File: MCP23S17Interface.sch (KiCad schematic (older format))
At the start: 8 parts, among them J1 Conn_01x09, J2 Conn_01x16, J3 Conn_01x03, J4 Conn_01x03, J5 Conn_01x03, U1 MCP23S17_SP

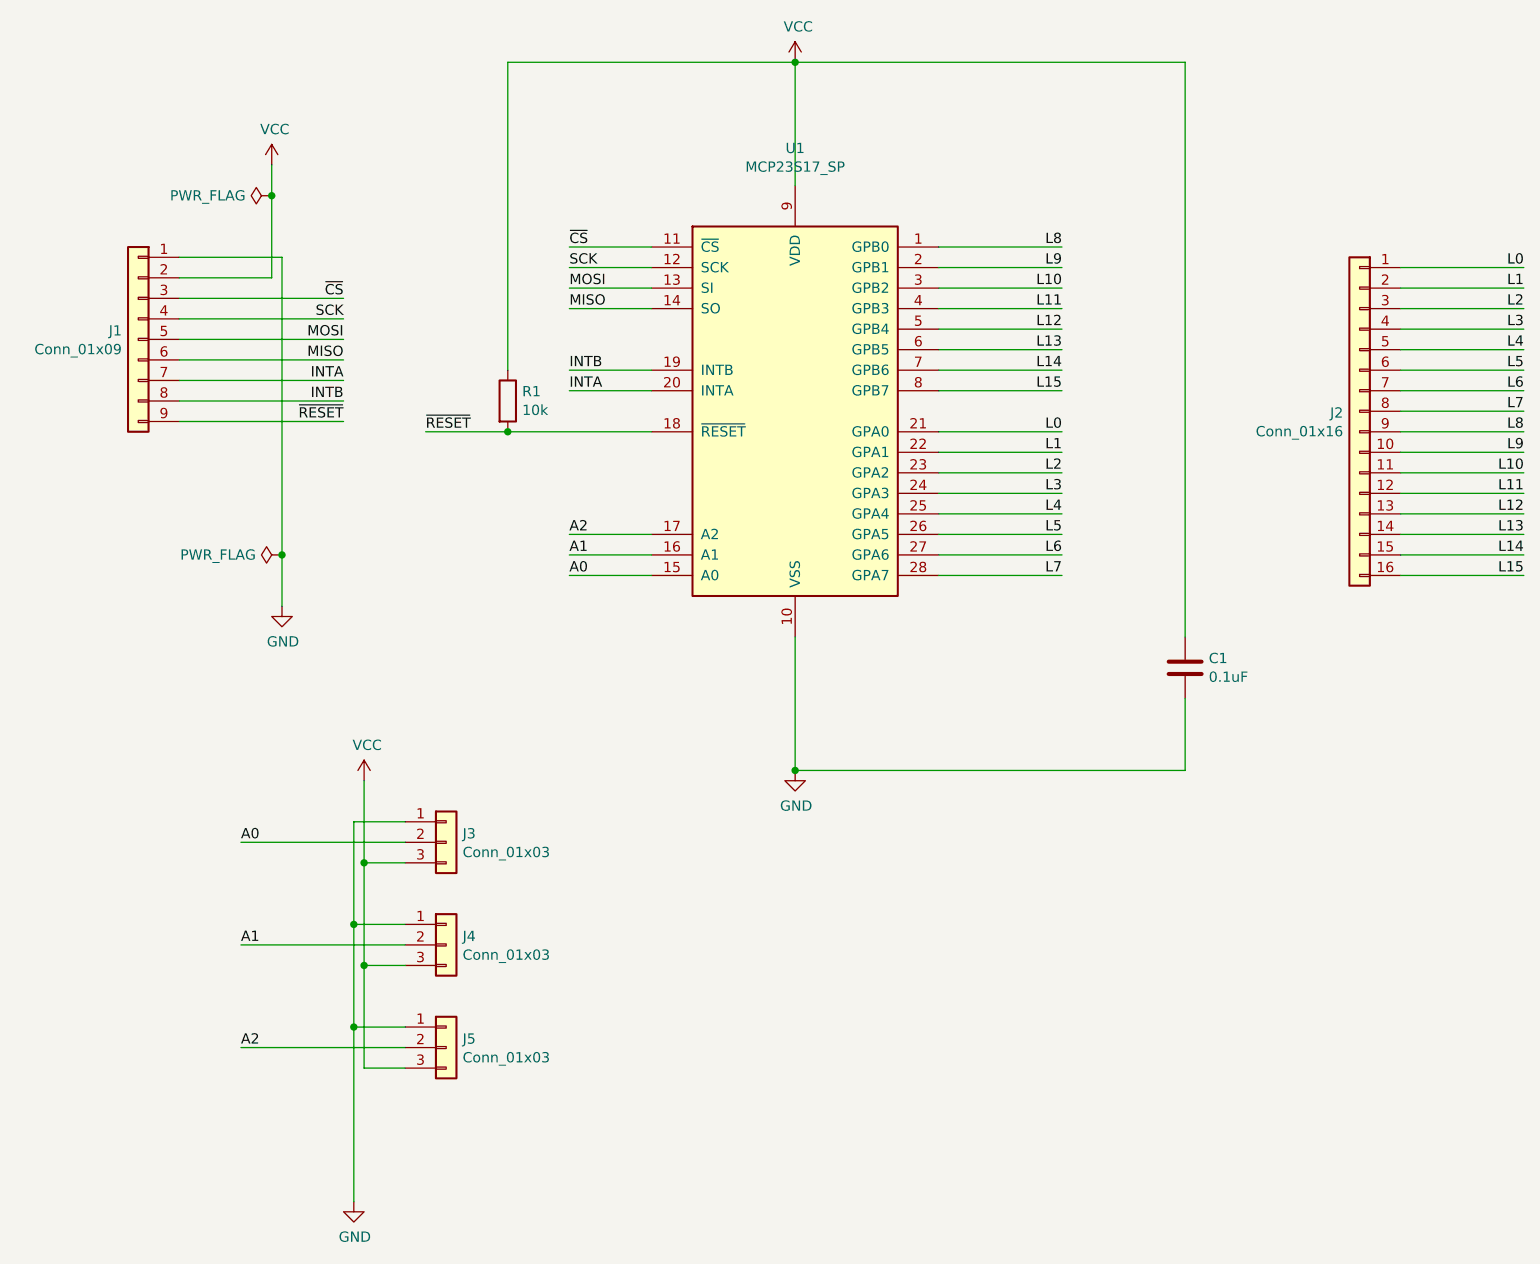
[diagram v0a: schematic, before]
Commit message: Replace the jumpered address selection with a dip switch box
Also, a 10k x 4 pull up resistor network in place of several 805 10k
resistors.
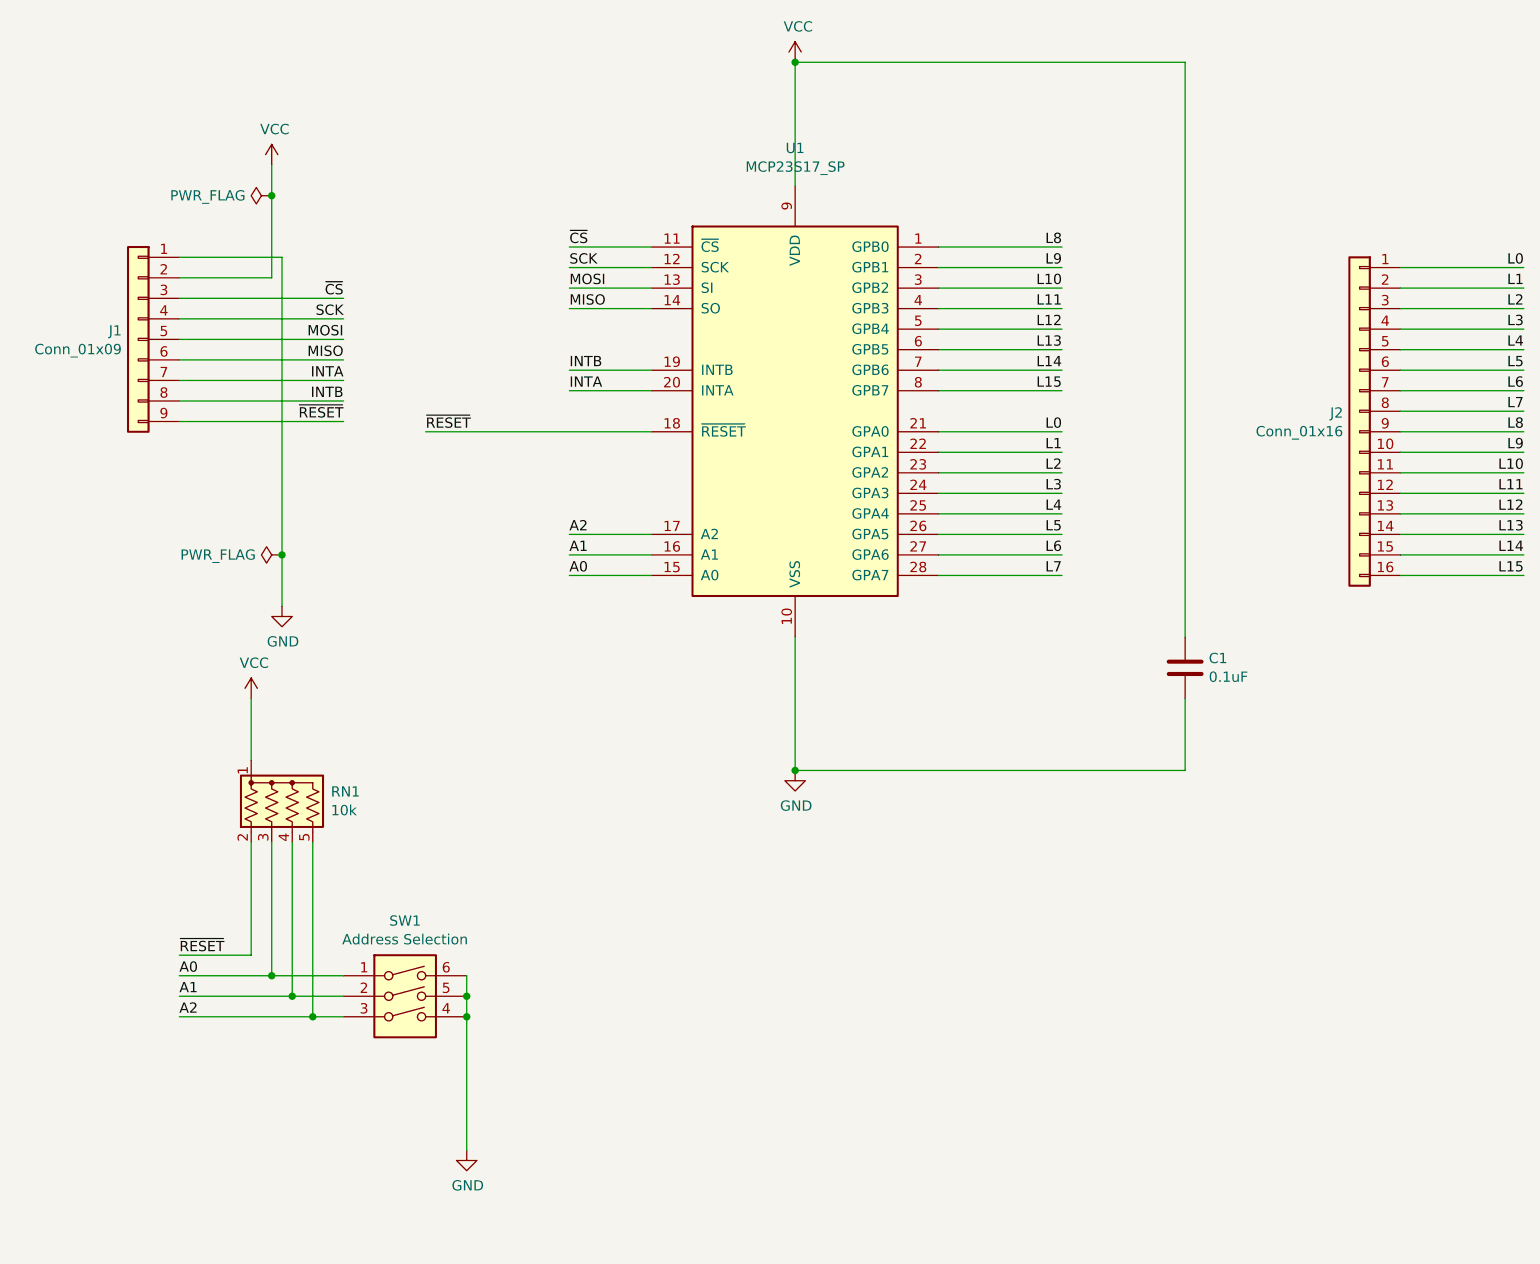
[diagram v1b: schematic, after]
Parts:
- removed J3, J4, J5: Conn_01x03, Connector_PinHeader_2.54mm:PinHeader_1x03_P2.54mm_Vertical, symbol Connector_Generic:Conn_01x03
- removed R1: 10k, Resistor_SMD:R_0805_2012Metric_Pad1.20x1.40mm_HandSolder, symbol Device:R
- added RN1: 10k, Resistor_THT:R_Array_SIP5, symbol Device:R_Network04_US
- added SW1: Address Selection, Switches:DIPSWITCH-03, symbol Switch:SW_DIP_x03
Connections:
- net A0: now also RN1.3 (R2), SW1.1
- net A1: now also RN1.4 (R3), SW1.2
- net A2: now also RN1.5 (R4), SW1.3
- net GND: now also SW1.4, SW1.5, SW1.6
- net VCC: now also RN1.1 (common)
- net ~RESET: now also RN1.2 (R1)
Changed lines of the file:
@@
 Wire Wire Line
 	3500 1800 3100 1800
-$Comp
-L Device:R R1
-U 1 1 5F9F82F2
-P 2800 2550
-F 0 "R1" H 2870 2596 50  0000 L CNN
-F 1 "10k" H 2870 2505 50  0000 L CNN
-F 2 "Resistor_SMD:R_0805_2012Metric_Pad1.20x1.40mm_HandSolder" V 2730 2550 50  0001 C CNN
-F 3 "~" H 2800 2550 50  0001 C CNN
-	1    2800 2550
-	1    0    0    -1
-$EndComp
-Wire Wire Line
-	2800 2700 3500 2700
-Wire Wire Line
-	2800 2400 2800 900
-Wire Wire Line
-	2800 900  4200 900
 Wire Wire Line
 	4200 900  4200 1500
-Wire Wire Line
-	2800 2700 2400 2700
-Connection ~ 2800 2700
 Text Label 2400 2700 0    50   ~ 0
 ~RESET
@@
 Text Label 2000 2550 2    50   ~ 0
 INTB
-Text Label 1500 4700 0    50   ~ 0
+Text Label 1200 5350 0    50   ~ 0
 A0
-Text Label 1500 5200 0    50   ~ 0
+Text Label 1200 5450 0    50   ~ 0
 A1
-Text Label 1500 5700 0    50   ~ 0
+Text Label 1200 5550 0    50   ~ 0
 A2
 Wire Wire Line
-	1500 5700 2300 5700
-Wire Wire Line
-	2300 5200 1500 5200
-Wire Wire Line
-	1500 4700 2300 4700
+	1200 5350 1650 5350
 Wire Wire Line
 	1200 2550 2000 2550
@@
 L15
 $Comp
-L Connector_Generic:Conn_01x03 J3
-U 1 1 5FCA39AF
-P 2500 4700
-F 0 "J3" H 2580 4742 50  0000 L CNN
-F 1 "Conn_01x03" H 2580 4651 50  0000 L CNN
-F 2 "Connector_PinHeader_2.54mm:PinHeader_1x03_P2.54mm_Vertical" H 2500 4700 50  0001 C CNN
-F 3 "~" H 2500 4700 50  0001 C CNN
-	1    2500 4700
-	1    0    0    -1
-$EndComp
-$Comp
-L Connector_Generic:Conn_01x03 J4
-U 1 1 5FCA73ED
-P 2500 5200
-F 0 "J4" H 2580 5242 50  0000 L CNN
-F 1 "Conn_01x03" H 2580 5151 50  0000 L CNN
-F 2 "Connector_PinHeader_2.54mm:PinHeader_1x03_P2.54mm_Vertical" H 2500 5200 50  0001 C CNN
-F 3 "~" H 2500 5200 50  0001 C CNN
-	1    2500 5200
-	1    0    0    -1
-$EndComp
-$Comp
-L Connector_Generic:Conn_01x03 J5
-U 1 1 5FCA956B
-P 2500 5700
-F 0 "J5" H 2580 5742 50  0000 L CNN
-F 1 "Conn_01x03" H 2580 5651 50  0000 L CNN
-F 2 "Connector_PinHeader_2.54mm:PinHeader_1x03_P2.54mm_Vertical" H 2500 5700 50  0001 C CNN
-F 3 "~" H 2500 5700 50  0001 C CNN
-	1    2500 5700
-	1    0    0    -1
-$EndComp
-Wire Wire Line
-	2300 4600 2050 4600
-Wire Wire Line
-	2050 4600 2050 5100
-Wire Wire Line
-	2300 4800 2100 4800
-Wire Wire Line
-	2100 4800 2100 4400
-Wire Wire Line
-	2300 5100 2050 5100
-Connection ~ 2050 5100
-Wire Wire Line
-	2300 5300 2100 5300
-Wire Wire Line
-	2100 5300 2100 4800
-Connection ~ 2100 4800
-Wire Wire Line
-	2300 5600 2050 5600
-Wire Wire Line
-	2050 5100 2050 5600
-Connection ~ 2050 5600
-Wire Wire Line
-	2050 5600 2050 6450
-Wire Wire Line
-	2300 5800 2100 5800
-Wire Wire Line
-	2100 5800 2100 5300
-Connection ~ 2100 5300
-$Comp
 L Connector_Generic:Conn_01x09 J1
 U 1 1 5FCB7AEE
@@
 $EndComp
 $Comp
-L power:VCC #PWR0101
-U 1 1 5FCBAF97
-P 2100 4400
-F 0 "#PWR0101" H 2100 4250 50  0001 C CNN
-F 1 "VCC" H 2115 4573 50  0000 C CNN
-F 2 "" H 2100 4400 50  0001 C CNN
-F 3 "" H 2100 4400 50  0001 C CNN
-	1    2100 4400
-	1    0    0    -1
-$EndComp
-$Comp
-L power:GND #PWR0102
-U 1 1 5FCBB539
-P 2050 6450
-F 0 "#PWR0102" H 2050 6200 50  0001 C CNN
-F 1 "GND" H 2055 6277 50  0000 C CNN
-F 2 "" H 2050 6450 50  0001 C CNN
-F 3 "" H 2050 6450 50  0001 C CNN
-	1    2050 6450
-	1    0    0    -1
-$EndComp
+L Switch:SW_DIP_x03 SW1
+U 1 1 5FB72829
+P 2300 5550
+F 0 "SW1" H 2300 6017 50  0000 C CNN
+F 1 "Address Selection" H 2300 5926 50  0000 C CNN
+F 2 "Switches:DIPSWITCH-03" H 2300 5550 50  0001 C CNN
+F 3 "~" H 2300 5550 50  0001 C CNN
+	1    2300 5550
+	1    0    0    -1
+$EndComp
+Wire Wire Line
+	2600 5350 2600 5450
+Connection ~ 2600 5450
+Wire Wire Line
+	2600 5450 2600 5550
+Connection ~ 2600 5550
+Wire Wire Line
+	2600 5550 2600 6200
+$Comp
+L power:GND #PWR06
+U 1 1 5FB7617A
+P 2600 6200
+F 0 "#PWR06" H 2600 5950 50  0001 C CNN
+F 1 "GND" H 2605 6027 50  0000 C CNN
+F 2 "" H 2600 6200 50  0001 C CNN
+F 3 "" H 2600 6200 50  0001 C CNN
+	1    2600 6200
+	1    0    0    -1
+$EndComp
+Wire Wire Line
+	2000 5450 1750 5450
+Wire Wire Line
+	1200 5550 1850 5550
+Wire Wire Line
+	2400 2700 3500 2700
+$Comp
+L Device:R_Network04_US RN1
+U 1 1 5FB8947C
+P 1750 4500
+F 0 "RN1" H 1938 4546 50  0000 L CNN
+F 1 "10k" H 1938 4455 50  0000 L CNN
+F 2 "Resistor_THT:R_Array_SIP5" V 2025 4500 50  0001 C CNN
+F 3 "http://www.vishay.com/docs/31509/csc.pdf" H 1750 4500 50  0001 C CNN
+	1    1750 4500
+	1    0    0    -1
+$EndComp
+Wire Wire Line
+	1550 4300 1550 4000
+$Comp
+L power:VCC #PWR05
+U 1 1 5FB8BBEE
+P 1550 4000
+F 0 "#PWR05" H 1550 3850 50  0001 C CNN
+F 1 "VCC" H 1565 4173 50  0000 C CNN
+F 2 "" H 1550 4000 50  0001 C CNN
+F 3 "" H 1550 4000 50  0001 C CNN
+	1    1550 4000
+	1    0    0    -1
+$EndComp
+Wire Wire Line
+	1550 4700 1550 5250
+Wire Wire Line
+	1550 5250 1200 5250
+Text Label 1200 5250 0    50   ~ 0
+~RESET
+Wire Wire Line
+	1650 4700 1650 5350
+Connection ~ 1650 5350
+Wire Wire Line
+	1650 5350 2000 5350
+Wire Wire Line
+	1750 4700 1750 5450
+Connection ~ 1750 5450
+Wire Wire Line
+	1750 5450 1200 5450
+Wire Wire Line
+	1850 4700 1850 5550
+Connection ~ 1850 5550
+Wire Wire Line
+	1850 5550 2000 5550
 $EndSCHEMATC

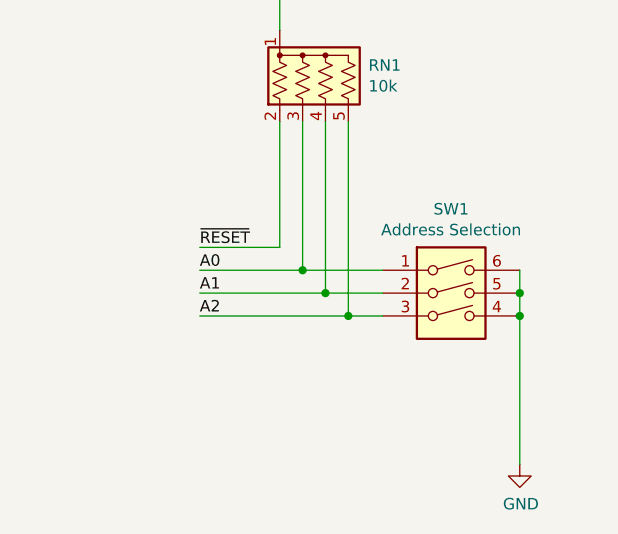
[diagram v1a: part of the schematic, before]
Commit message: Start working on the new PCB
Rearrange ordering of dip switches to make routing easier
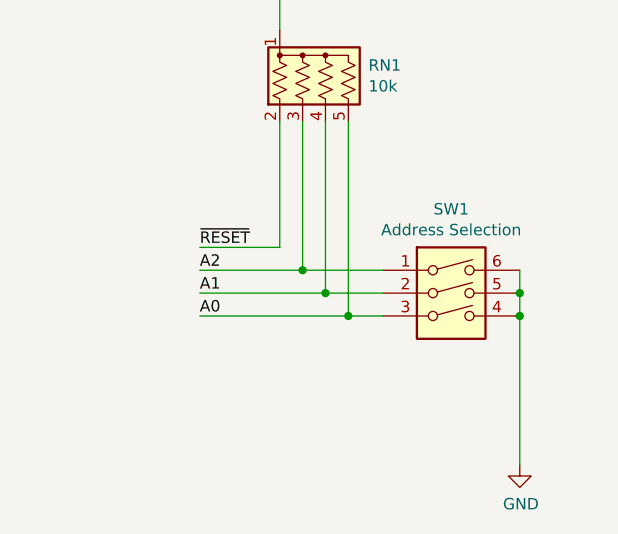
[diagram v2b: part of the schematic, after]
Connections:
- net A0: now also RN1.5 (R4), SW1.3; no longer RN1.3 (R2), SW1.1
- net A2: now also RN1.3 (R2), SW1.1; no longer RN1.5 (R4), SW1.3
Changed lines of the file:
@@
 Text Label 2000 2550 2    50   ~ 0
 INTB
-Text Label 1200 5350 0    50   ~ 0
+Text Label 1200 5550 0    50   ~ 0
 A0
 Text Label 1200 5450 0    50   ~ 0
 A1
-Text Label 1200 5550 0    50   ~ 0
+Text Label 1200 5350 0    50   ~ 0
 A2
 Wire Wire Line

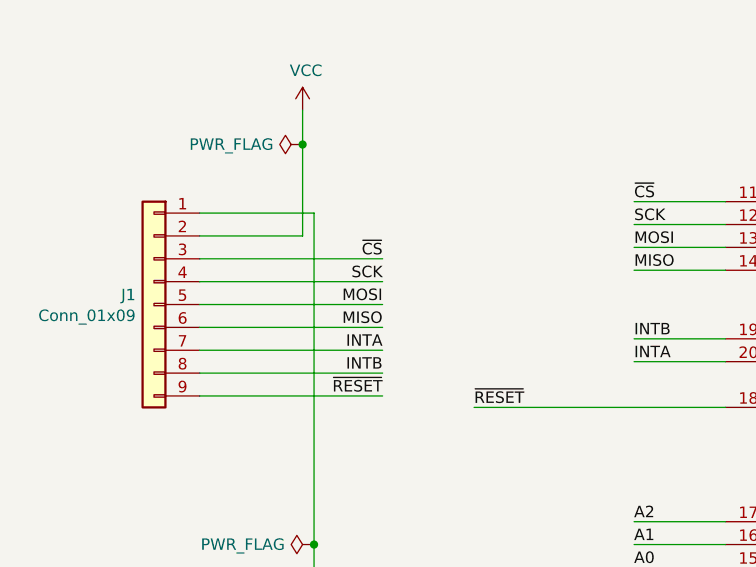
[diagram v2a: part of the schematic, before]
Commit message: Rearrange lines further to reduce trace fanout
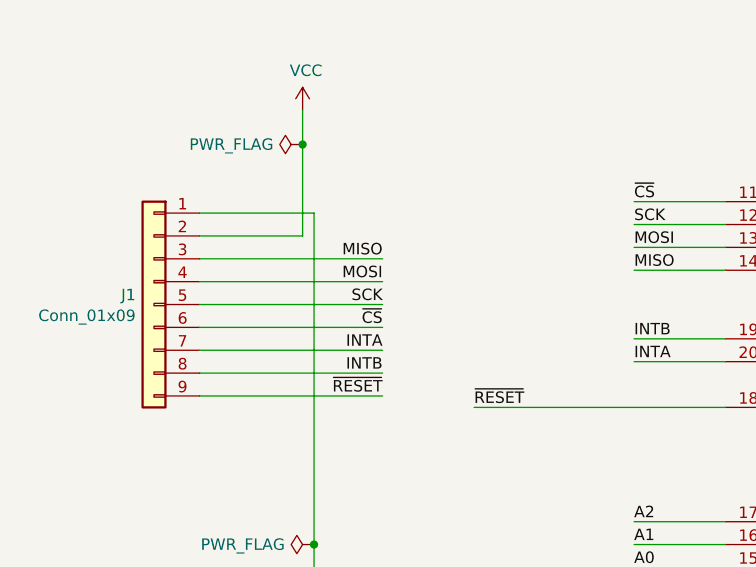
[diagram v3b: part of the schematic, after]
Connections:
- net MISO: now also J1.3 (Pin_3); no longer J1.6 (Pin_6)
- net MOSI: now also J1.4 (Pin_4); no longer J1.5 (Pin_5)
- net SCK: now also J1.5 (Pin_5); no longer J1.4 (Pin_4)
- net ~CS: now also J1.6 (Pin_6); no longer J1.3 (Pin_3)
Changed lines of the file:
@@
 	1    0    0    -1
 $EndComp
+Text Label 2000 2350 2    50   ~ 0
+~CS
+Text Label 2000 2250 2    50   ~ 0
+SCK
+Text Label 2000 2150 2    50   ~ 0
+MOSI
 Text Label 2000 2050 2    50   ~ 0
-~CS
-Text Label 2000 2150 2    50   ~ 0
-SCK
-Text Label 2000 2250 2    50   ~ 0
-MOSI
-Text Label 2000 2350 2    50   ~ 0
 MISO
 Text Label 2000 2650 2    50   ~ 0
